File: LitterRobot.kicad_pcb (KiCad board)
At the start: 4 copper layers, 0 parts

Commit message: Add the board outline
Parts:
- added REF**: TestPoint_Pad_2.0x2.0mm, TestPoint:TestPoint_Pad_2.0x2.0mm, F.Cu at (80.0, 50.0)
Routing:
- net GND: vias 0 -> 26
- added copper zone on B.Cu, net GND
- added copper zone on F.Cu, net GND
- added copper zone on In1.Cu, net GND
- added copper zone on In2.Cu, net GND
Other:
- board outline added: 55 x 140 mm

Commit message: Place the main components on the PCB
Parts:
- removed REF**: TestPoint_Pad_2.0x2.0mm, TestPoint:TestPoint_Pad_2.0x2.0mm
- added D1: SMLVN6RGB1U, LitterRobot:ROHM_SMLVN6, B.Cu at (114.0, 168.0)
- added D2: SMLVN6RGB1U, LitterRobot:ROHM_SMLVN6, B.Cu at (79.2, 147.9)
- added D3: SMLVN6RGB1U, LitterRobot:ROHM_SMLVN6, B.Cu at (96.6, 157.9)
- added D4: SMLVN6RGB1U, LitterRobot:ROHM_SMLVN6, B.Cu at (79.3, 63.6)
- added D5: SMLVN6RGB1U, LitterRobot:ROHM_SMLVN6, B.Cu at (86.8, 129.5)
- added D6: SMLVN6RGB1U, LitterRobot:ROHM_SMLVN6, B.Cu at (84.8, 99.0)
- added D7: SMLVN6RGB1U, LitterRobot:ROHM_SMLVN6, B.Cu at (74.9, 39.5)
- added H1: MountingHole, MountingHole:MountingHole_4mm, F.Cu at (73.5, 73.4)
- added H2: MountingHole, MountingHole:MountingHole_4mm, F.Cu at (88.0, 83.4)
- added H3: MountingHole, MountingHole:MountingHole_4mm, F.Cu at (92.0, 111.0)
- added H4: MountingHole, MountingHole:MountingHole_4mm, F.Cu at (73.3, 134.5)
- added H5: MountingHole, MountingHole:MountingHole_4mm, F.Cu at (97.0, 148.1)
- added J1: DF11C-4DP-2V(57), LitterRobot:Hirose_DF11C-4DP-2V(57), F.Cu at (75.5, 153.9)
- added J2: DF11C-6DP-2V(57), LitterRobot:Hirose_DF11C-6DP-2V(57), F.Cu at (86.4, 159.0)
- added J3: DF11C-8DP-2V(57), LitterRobot:Hirose_DF11C-8DP-2V(57), F.Cu at (97.3, 164.1)
- added J4: DF11C-6DP-2V(57), LitterRobot:Hirose_DF11C-6DP-2V(57), F.Cu at (110.2, 165.8)
- added SW1: PCB_Push_Button, LitterRobot:PCB_Push_Button_5mm_0.4mm, B.Cu at (81.0, 96.7)
- added SW2: PCB_Push_Button, LitterRobot:PCB_Push_Button_5mm_0.4mm, B.Cu at (78.8, 41.8)
- added SW3: PCB_Push_Button, LitterRobot:PCB_Push_Button_5mm_0.4mm, B.Cu at (83.2, 65.9)
- added SW4: PCB_Push_Button, LitterRobot:PCB_Push_Button_5mm_0.4mm, B.Cu at (75.4, 61.4)
- added SW5: PCB_Push_Button, LitterRobot:PCB_Push_Button_5mm_0.4mm, B.Cu at (90.7, 131.8)
- added SW6: PCB_Push_Button, LitterRobot:PCB_Push_Button_5mm_0.4mm, B.Cu at (82.9, 127.2)
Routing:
- net +3V3: vias 0 -> 6
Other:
- outline, holes or cut-outs redrawn

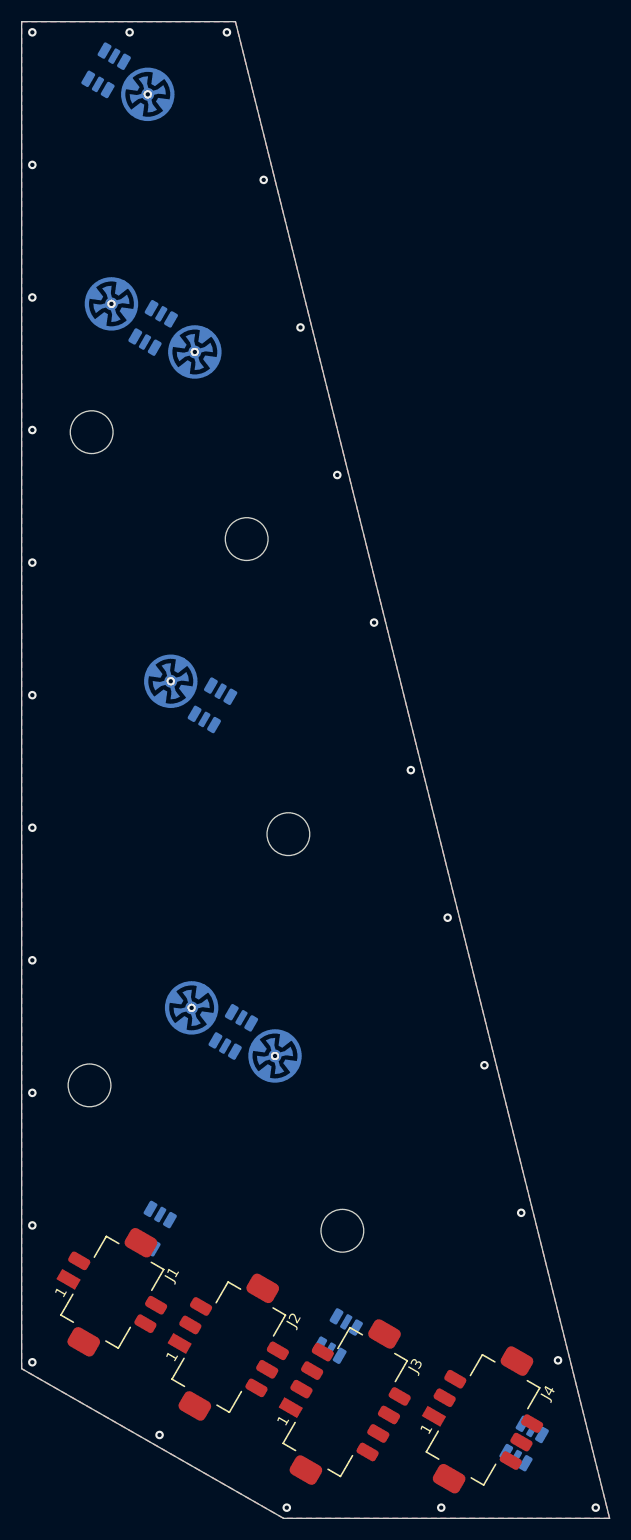
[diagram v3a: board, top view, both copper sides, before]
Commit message: Add an ambient light sensor
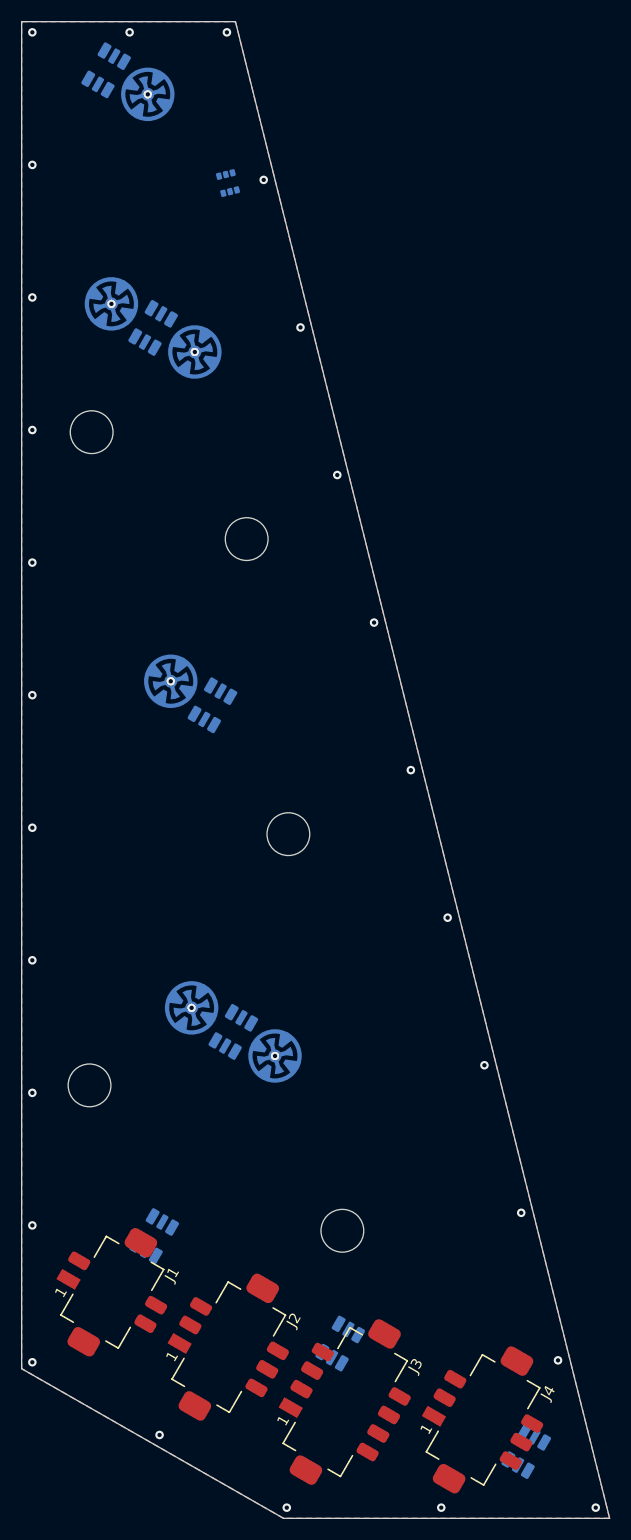
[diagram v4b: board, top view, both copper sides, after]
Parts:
- added U3: VEML6035, LitterRobot:Vishay_VEML6035, B.Cu at (86.3, 50.1)
- moved D3 0.73 mm to (96.8, 158.7)
- moved D1 0.73 mm to (114.2, 168.7)
- moved D2 0.73 mm to (79.4, 148.6)
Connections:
- net /Control panel/Cycle_Button renamed /Cycle_button
- net /Control panel/Empty_Button renamed /Empty_button
- net /Control panel/Power_Button renamed /Power_button
- net /Control panel/Reset_Button renamed /Reset_button
- J1 pad 1: (no net) -> +3V3
- J1 pad 4: (no net) -> GND
- J2 pad 1: +15V -> Net-(F1-Pad2)
- J2 pad 4: (no net) -> GND
- J3 pad 1: +7V -> (no net)
- J3 pad 8: GND -> (no net)
- J4 pad 1: (no net) -> +15V
- J4 pad 6: (no net) -> GND
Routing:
- added copper zone on In1.Cu, net +3V3
- removed copper zone on In1.Cu, net GND

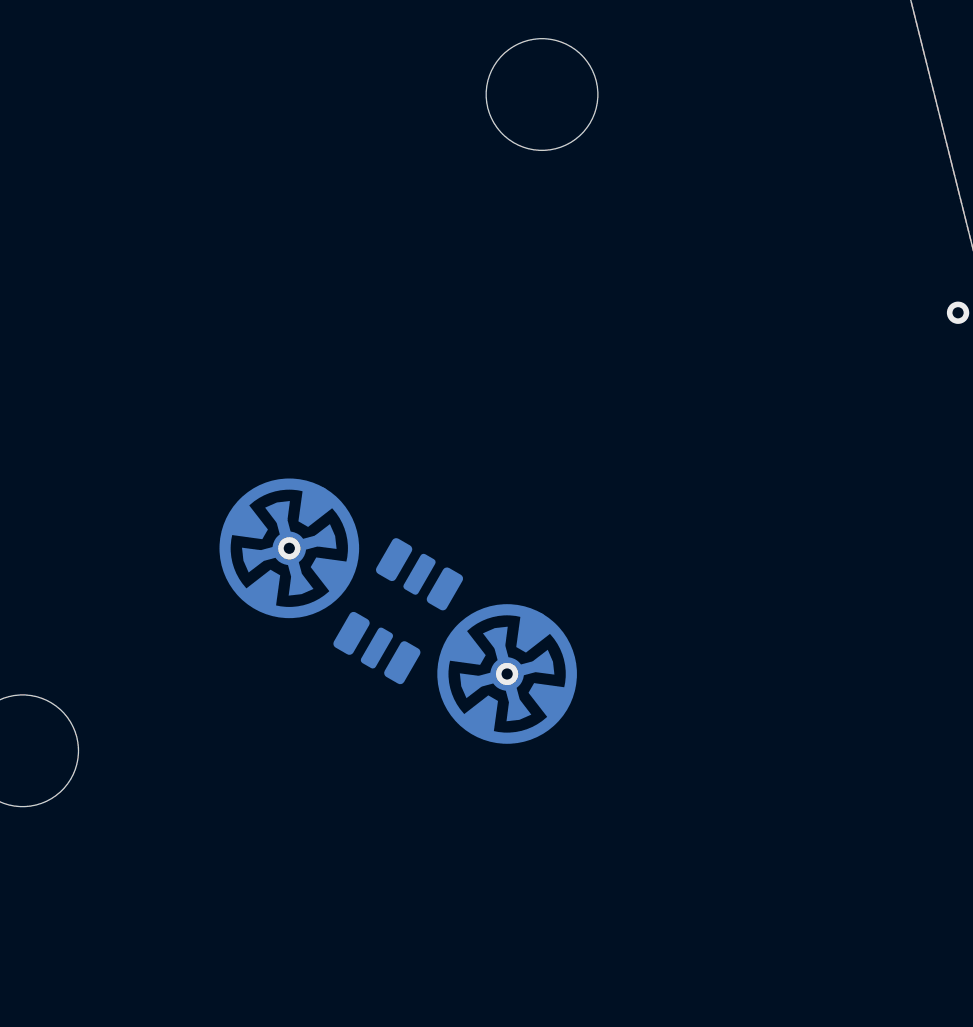
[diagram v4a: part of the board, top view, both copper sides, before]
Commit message: Add the FPGA footprint
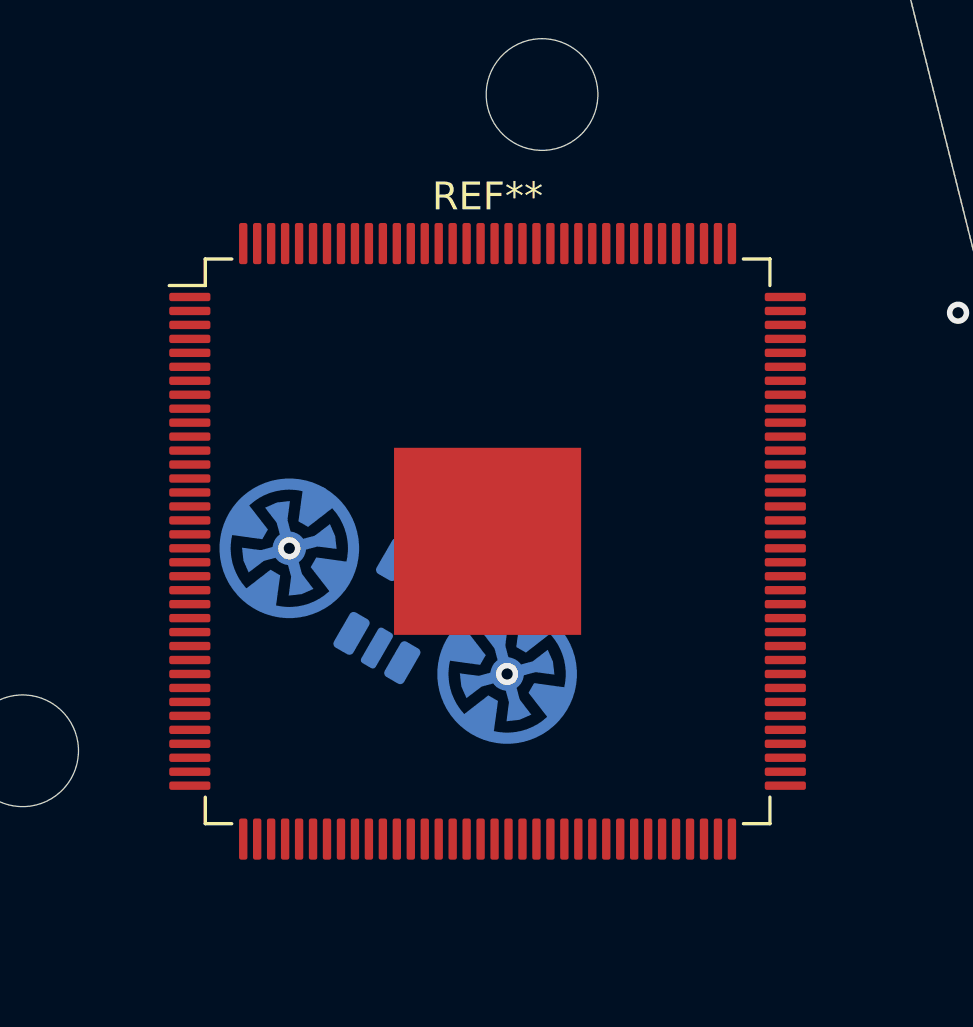
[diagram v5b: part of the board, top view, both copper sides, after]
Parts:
- added REF**: Intel_EQFP-144-1EP_20x20mm_P0.5mm_EP6.7x6.7mm, LitterRobot:Intel_EQFP-144-1EP_20x20mm_P0.5mm_EP6.7x6.7mm, F.Cu at (90.0, 127.0)

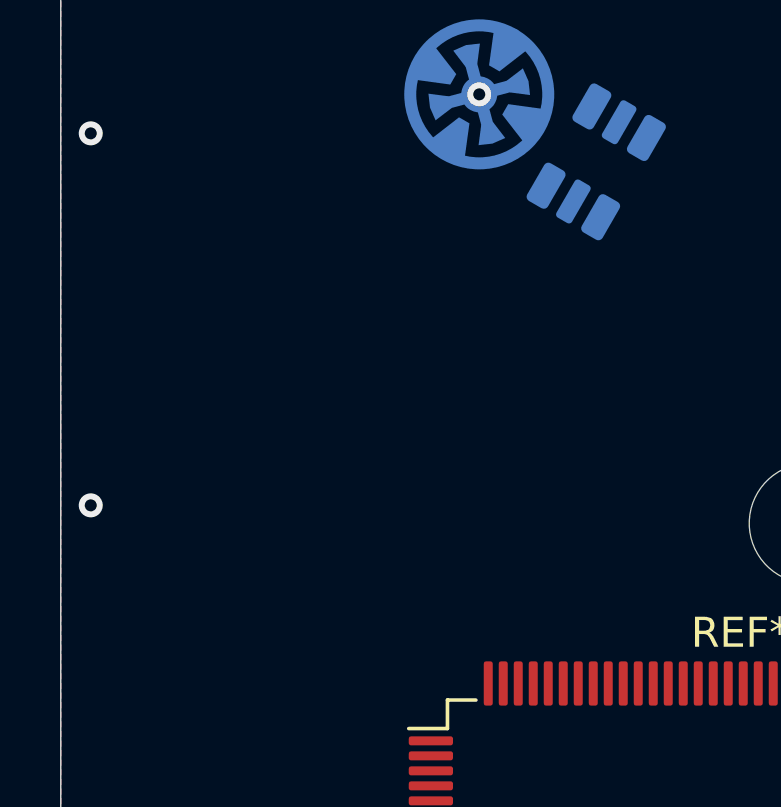
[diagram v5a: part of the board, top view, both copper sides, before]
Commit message: Add support components for the FPGA
- Configuration EEPROM
- 20 MHz oscillator
- JTAG debug port connector
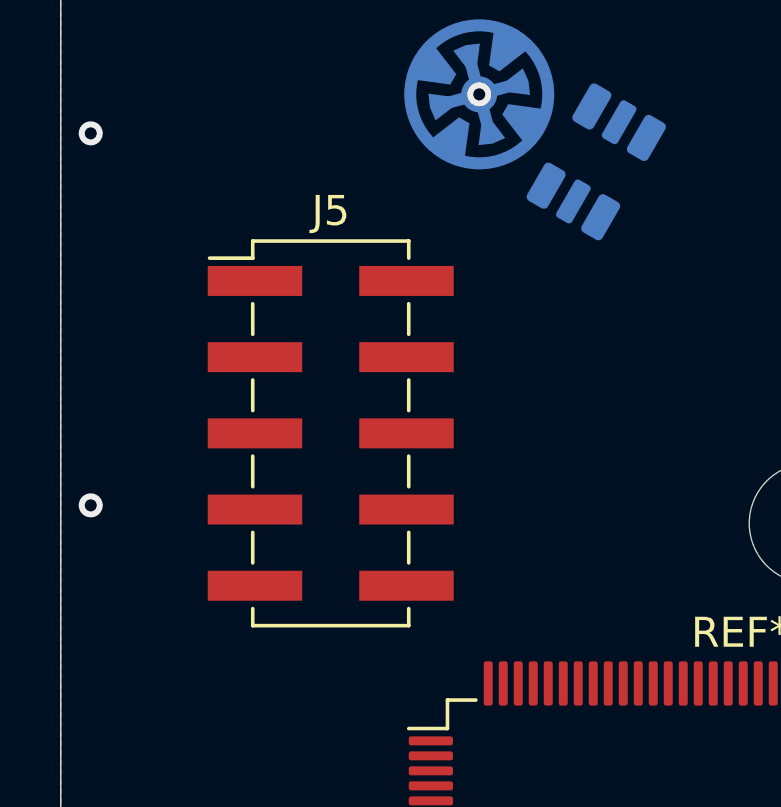
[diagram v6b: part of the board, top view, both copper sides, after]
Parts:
- added J5: Conn_02x05_Odd_Even, Connector_PinHeader_2.54mm:PinHeader_2x05_P2.54mm_Vertical_SMD, F.Cu at (76.0, 108.0)
